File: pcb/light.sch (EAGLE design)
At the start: 6 parts, among them J3 FFC3B07-05-T

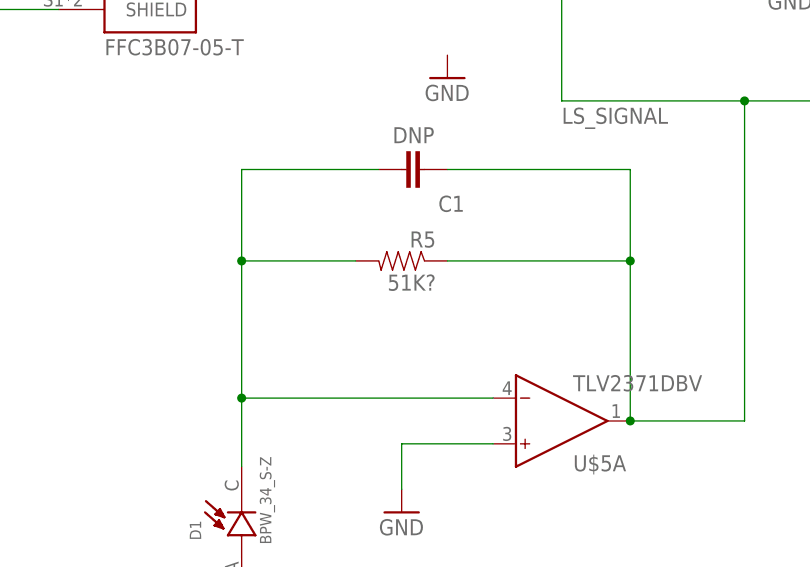
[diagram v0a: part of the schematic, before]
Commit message: adjusted gain resistor values, added more captures
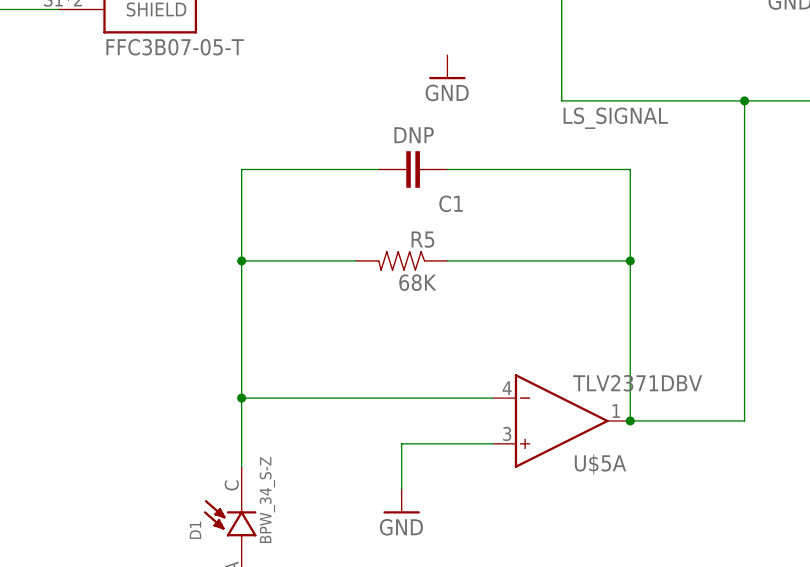
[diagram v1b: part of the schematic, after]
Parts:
- R5: value 51K? -> 68K
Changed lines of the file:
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@@
 <part name="GND2" library="SparkFun" deviceset="GND" device=""/>
 <part name="+3V1" library="supply1" library_urn="urn:adsk.eagle:library:371" deviceset="+3V3" device=""/>
-<part name="R5" library="joyAnalog" deviceset="RESISTOR" device="0805-RES" value="51K?"/>
+<part name="R5" library="joyAnalog" deviceset="RESISTOR" device="0805-RES" value="68K"/>
 <part name="C1" library="clock" deviceset="CAP" device="0805" value="DNP"/>
 <part name="GND4" library="SparkFun" deviceset="GND" device=""/>
